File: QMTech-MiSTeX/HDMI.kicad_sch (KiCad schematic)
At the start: 33 parts, among them U1 ADV7513BSWZ, U2 TPS76318

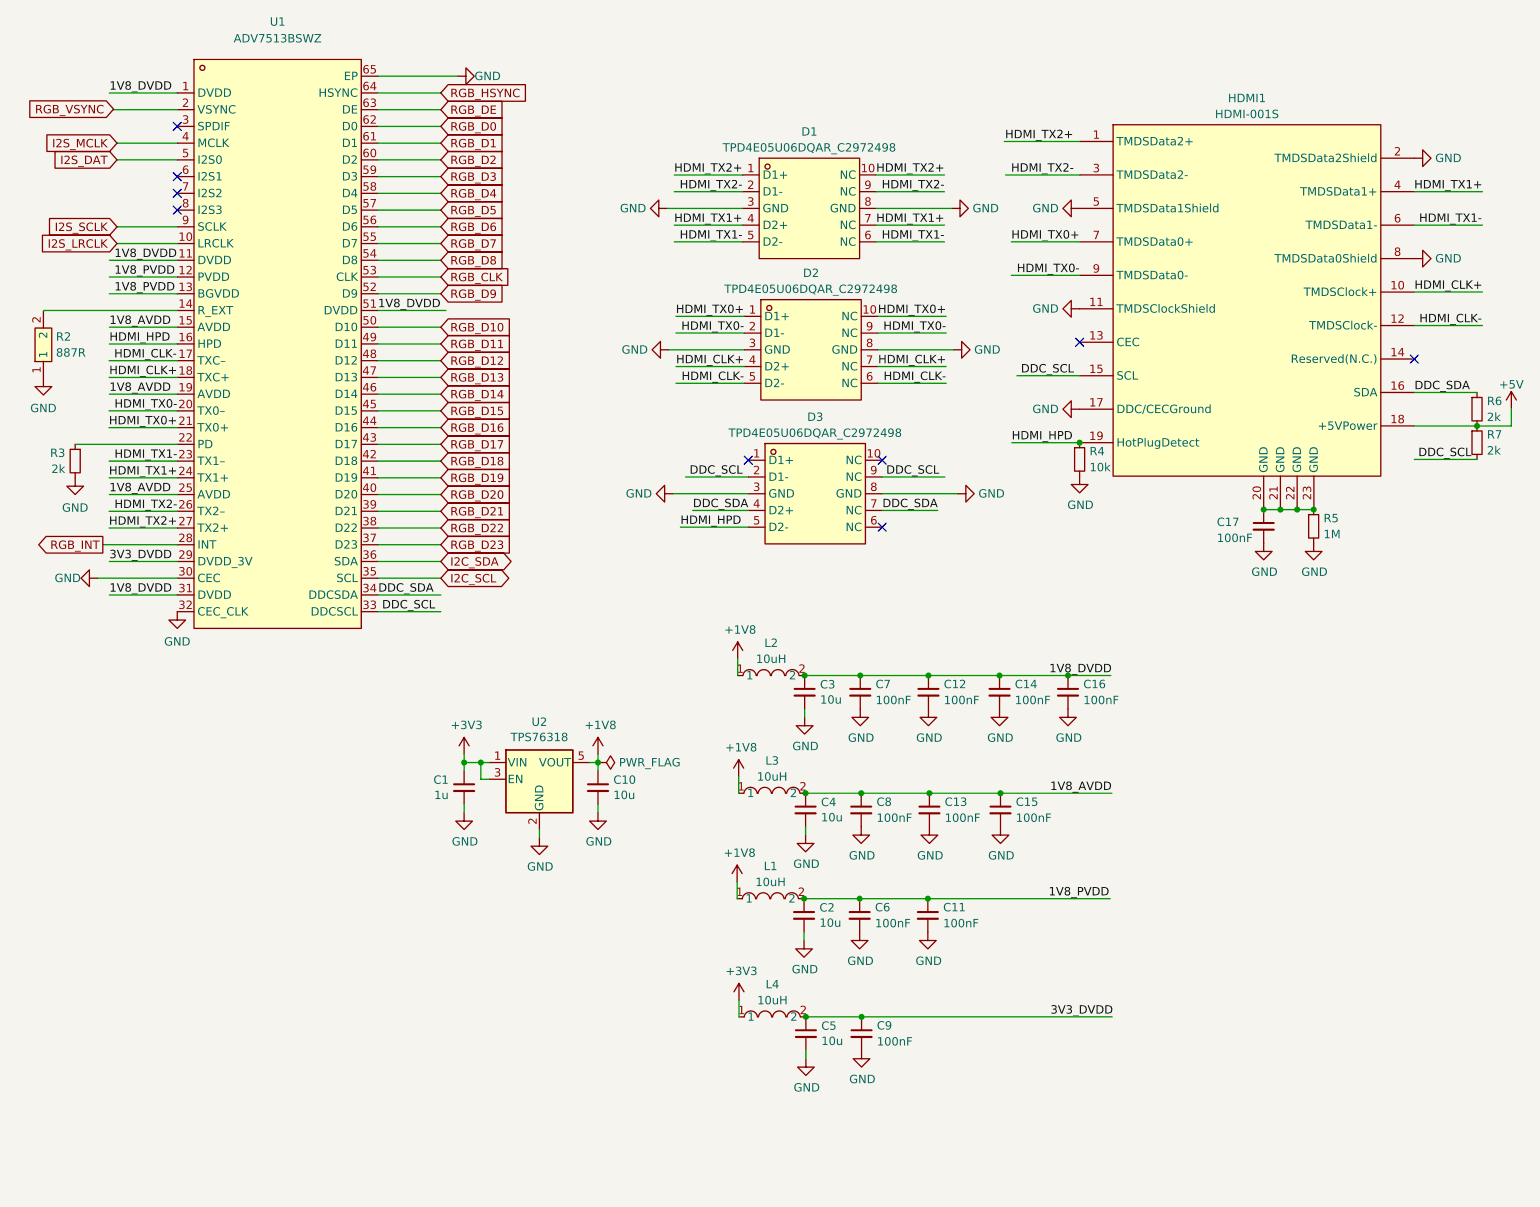
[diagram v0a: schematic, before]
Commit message: show the schematic borders and fix the design to fit
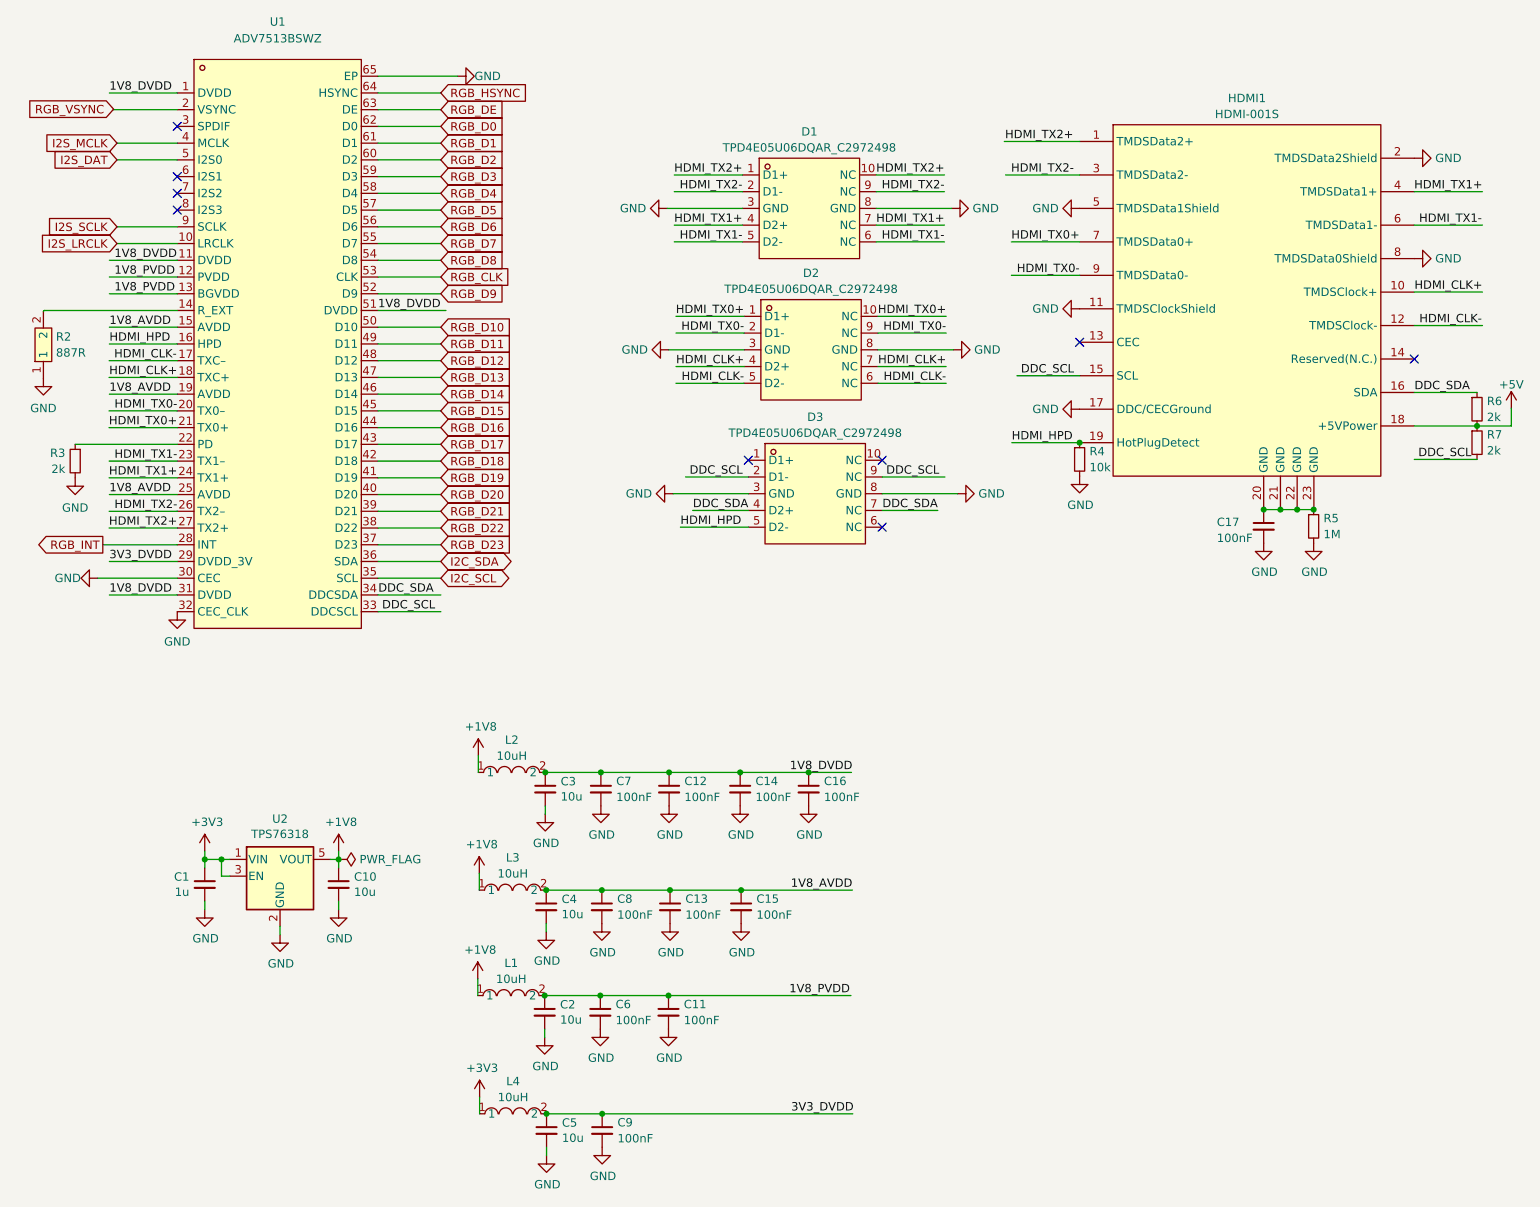
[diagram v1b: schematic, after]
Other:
- moved on the sheet: C1, C10, C11, C12, C13, C14, C15, C16, C2, C3, C4, C5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
